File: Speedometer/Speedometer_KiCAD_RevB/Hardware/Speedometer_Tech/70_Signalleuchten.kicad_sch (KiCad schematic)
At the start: 13 parts, among them U700 WS2812B-4020_2, U701 WS2812B-4020_2, U702 WS2812B-4020_2, U703 WS2812B-4020_2, U704 WS2812B-4020_2, U705 WS2812B-4020_2, U706 WS2812B-4020_2, U707 WS2812B-4020_2, U708 WS2812B-4020_2, U709 WS2812B-4020_2, U710 WS2812B-4020_2, U711 WS2812B-4020_2, U712 WS2812B-4020_2

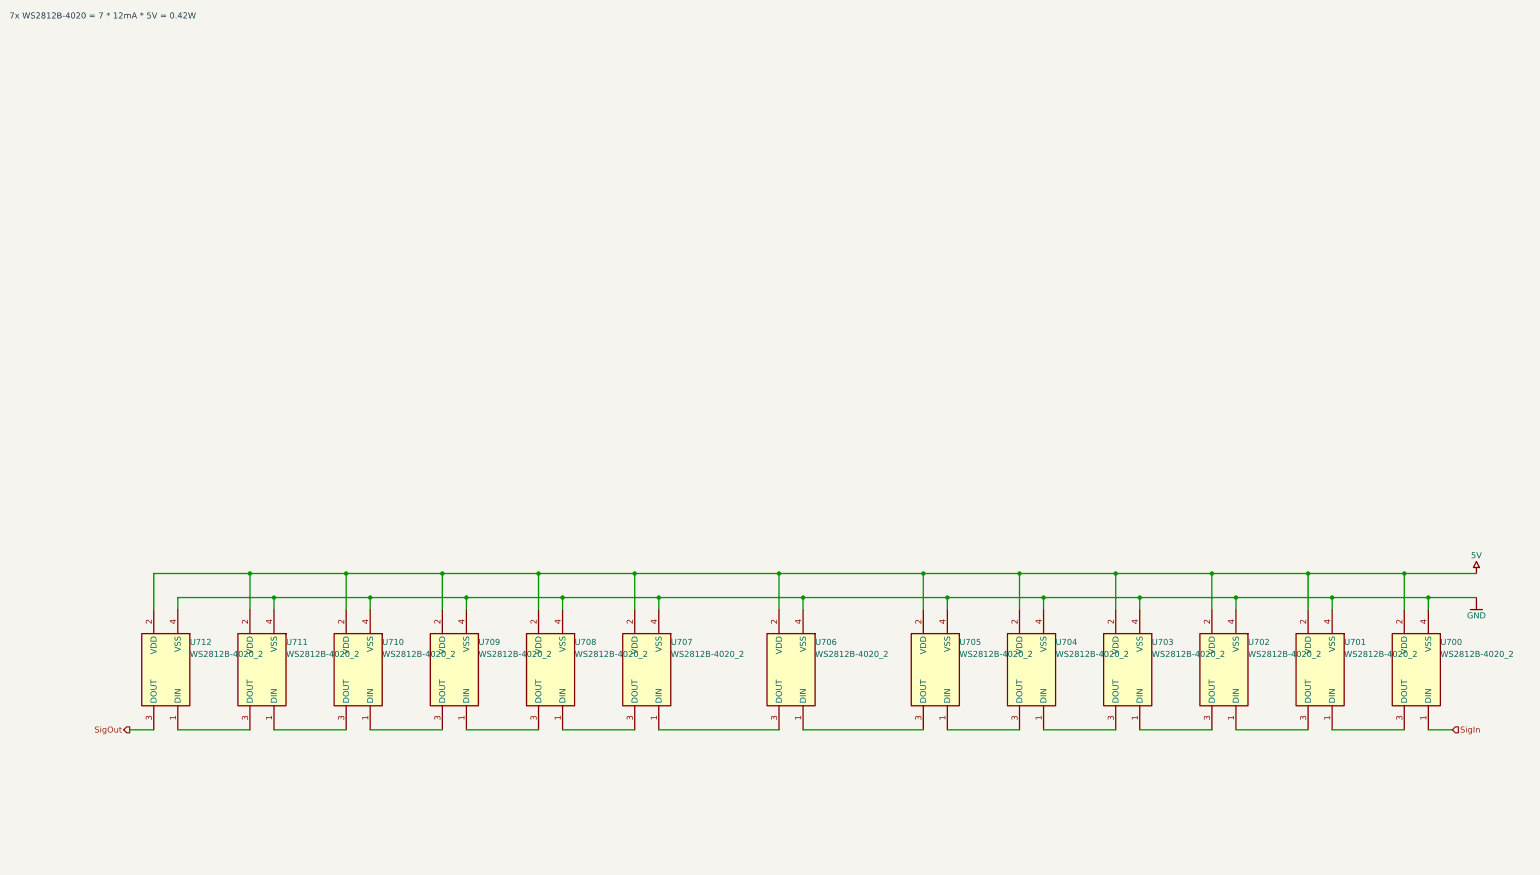
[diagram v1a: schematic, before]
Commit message: current version of lada speedometer in kicad
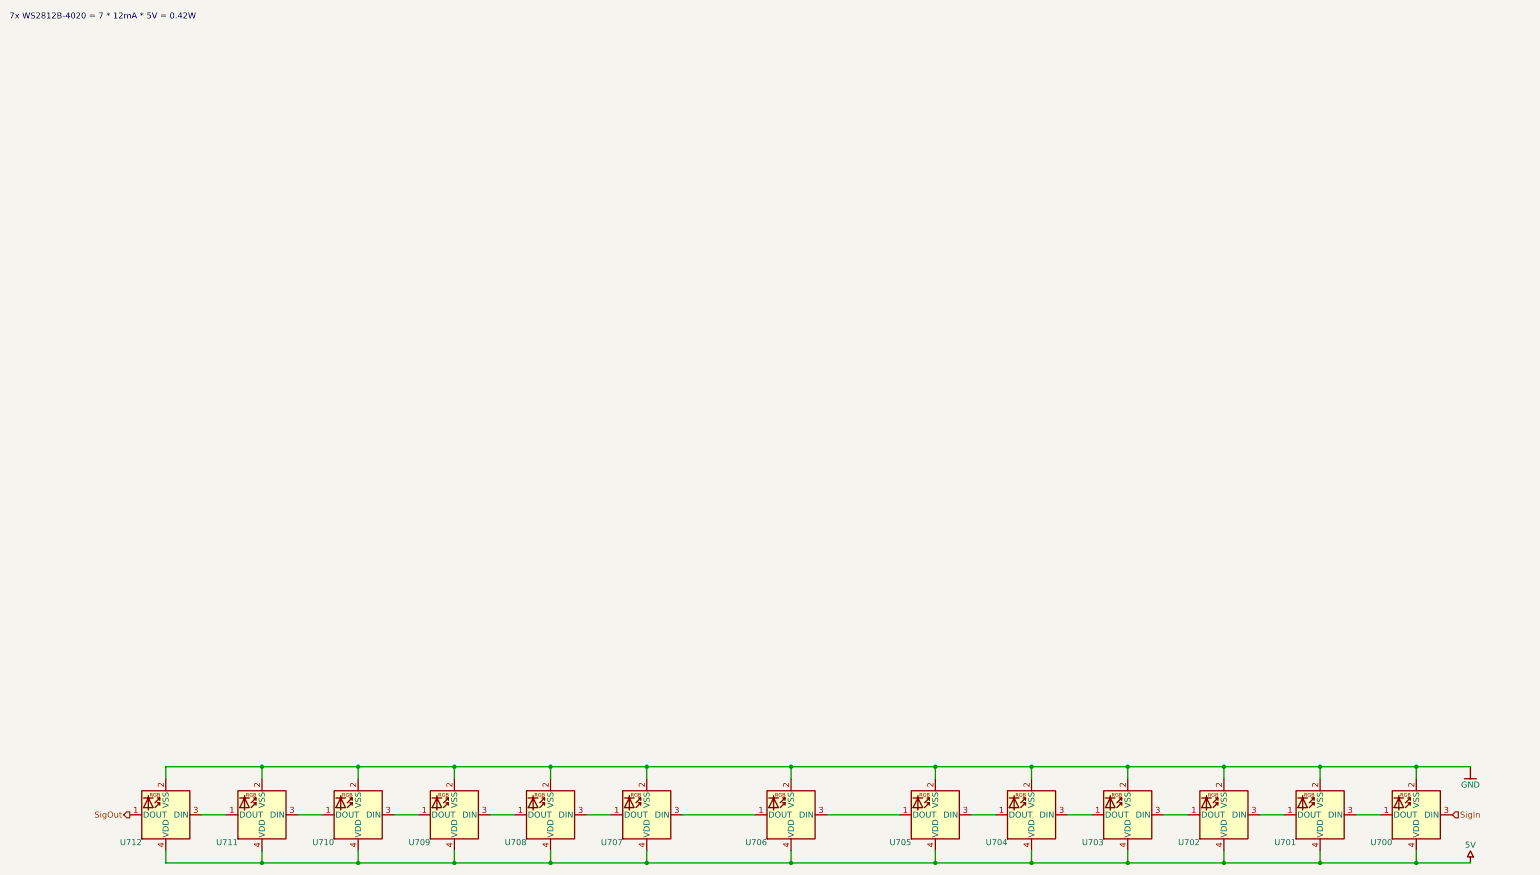
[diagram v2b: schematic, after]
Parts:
- removed U700, U701, U702, U703, U704, U705, U706, U707, U708, U709, U710, U711, U712: WS2812B-4020_2, LED_WS2812B-4020, symbol Speedometer_Tech-altium-import:Designator_1_WS2812B-4020_2
- added U700, U701, U702, U703, U704, U705, U706, U707, U708, U709, U710, U711, U712: WS2812B-4020_2, LED_SMD:LED_WS2812B-2020_PLCC4_2.0x2.0mm, symbol LED:WS2812B-2020
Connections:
- net 5V: now also U700.4 (VDD), U701.4 (VDD), U702.4 (VDD), U703.4 (VDD), U704.4 (VDD), U705.4 (VDD), U706.4 (VDD), U707.4 (VDD), U708.4 (VDD), U709.4 (VDD), U710.4 (VDD), U711.4 (VDD), U712.4 (VDD)
- net GND: now also U700.2 (VSS), U701.2 (VSS), U702.2 (VSS), U703.2 (VSS), U704.2 (VSS), U705.2 (VSS), U706.2 (VSS), U707.2 (VSS), U708.2 (VSS), U709.2 (VSS), U710.2 (VSS), U711.2 (VSS), U712.2 (VSS)
- net SigIn: now also U700.3 (DIN)
- net SigOut: now also U712.1 (DOUT)
- new net: U708.1 (DOUT), U709.3 (DIN)
- new net: U707.1 (DOUT), U708.3 (DIN)
- new net: U710.1 (DOUT), U711.3 (DIN)
- new net: U709.1 (DOUT), U710.3 (DIN)
- new net: U706.1 (DOUT), U707.3 (DIN)
- new net: U701.1 (DOUT), U702.3 (DIN)
- new net: U700.1 (DOUT), U701.3 (DIN)
- new net: U711.1 (DOUT), U712.3 (DIN)
- new net: U704.1 (DOUT), U705.3 (DIN)
- new net: U703.1 (DOUT), U704.3 (DIN)
- new net: U702.1 (DOUT), U703.3 (DIN)
- new net: U705.1 (DOUT), U706.3 (DIN)
